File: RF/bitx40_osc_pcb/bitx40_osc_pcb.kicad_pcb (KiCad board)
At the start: 2 copper layers, 16 parts, among them J1 Alim 5V, J2 Variable Capacitor, J3 Oscillator Output, Q1 2N3904, Q2 2N3904

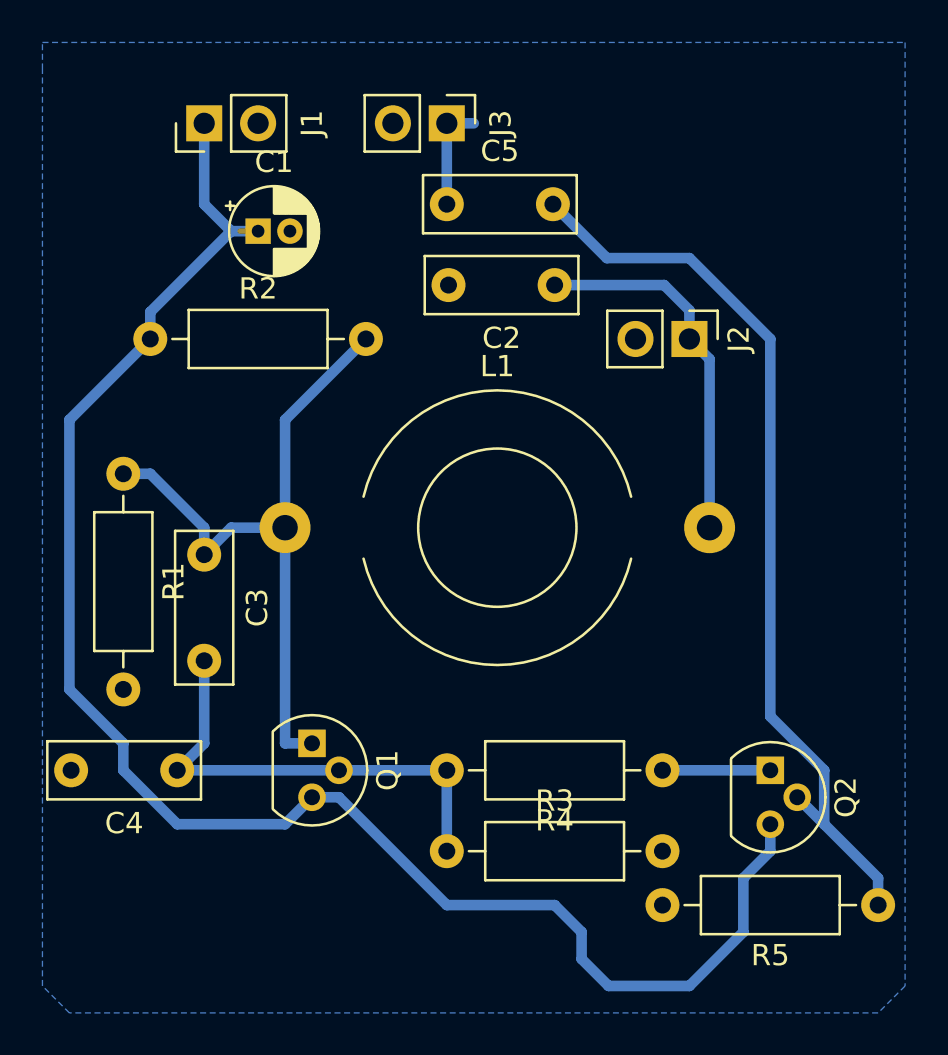
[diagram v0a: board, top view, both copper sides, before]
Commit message: Correct 2N3904 package & review (ok)
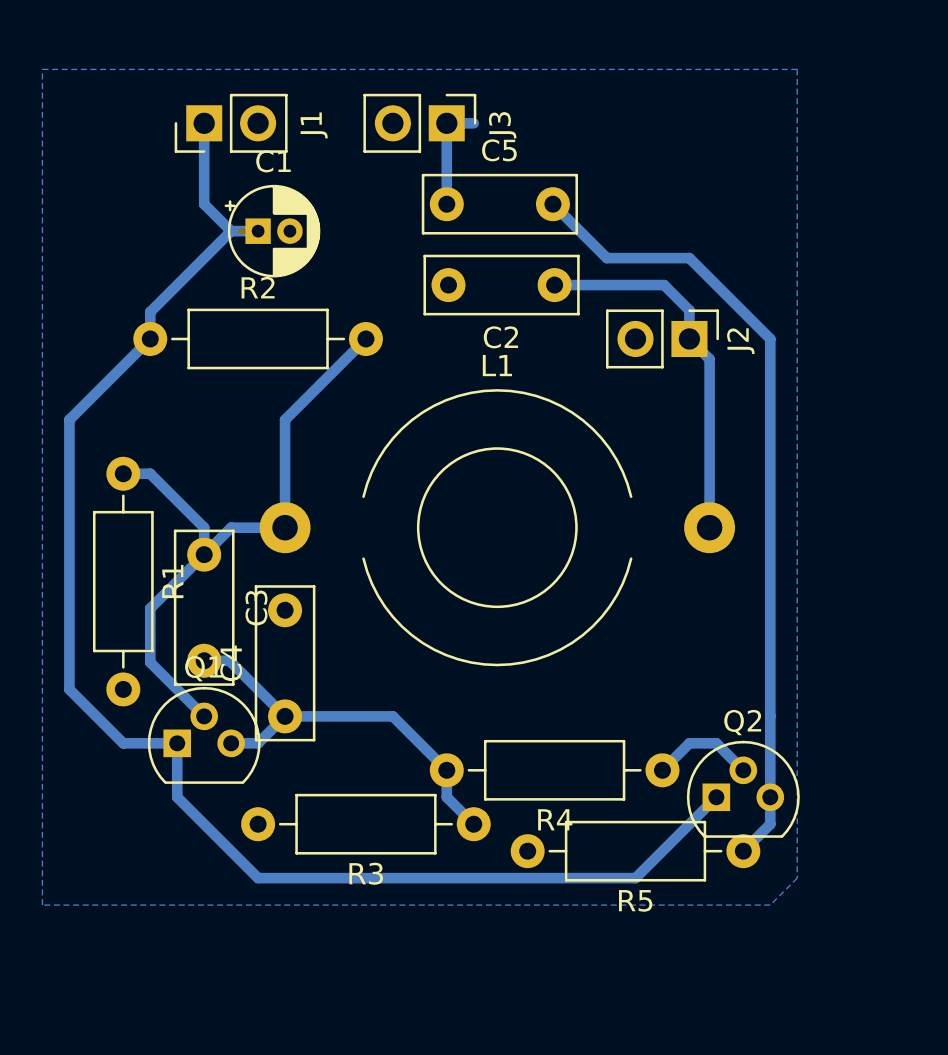
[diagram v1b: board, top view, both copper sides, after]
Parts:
- moved R5 6.84 mm to (182.9, 61.0)
- moved Q1 6.35 mm to (156.2, 55.9), turned to 0 degrees
- moved C4 5.68 mm to (161.3, 54.6), turned to 90 degrees
- moved Q2 2.84 mm to (181.6, 58.4), turned to 0 degrees
- moved R3 1.80 mm to (170.2, 59.7), turned to 180 degrees
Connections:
- Q1 pad 1: Net-(C3-Pad1) -> +5V
- Q1 pad 2: Net-(C3-Pad2) -> Net-(C3-Pad1)
- Q1 pad 3: +5V -> Net-(C3-Pad2)
- Q2 pad 1: Net-(Q2-Pad1) -> +5V
- Q2 pad 2: Net-(C5-Pad2) -> Net-(Q2-Pad2)
- Q2 pad 3: +5V -> Net-(C5-Pad2)
- R4 pad 1: Net-(Q2-Pad1) -> Net-(Q2-Pad2)
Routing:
- net +5V: track 79.2 -> 69.7 mm
- net Net-(C5-Pad2): track 43.4 -> 37.5 mm
- net Net-(Q2-Pad1): track 5.08 -> 0.00 mm
- net Net-(Q2-Pad2): track 0.00 -> 4.86 mm
- net Net-(C3-Pad2): track 22.2 -> 19.7 mm
- net Net-(C3-Pad1): track 32.4 -> 30.7 mm
